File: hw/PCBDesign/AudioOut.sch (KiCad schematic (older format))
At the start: 1 part

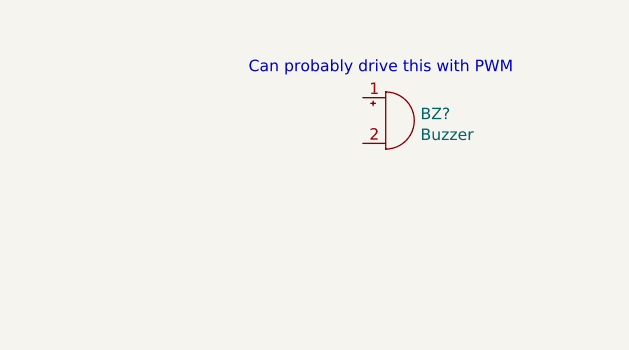
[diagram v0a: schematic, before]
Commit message: Add HMI input circuitry
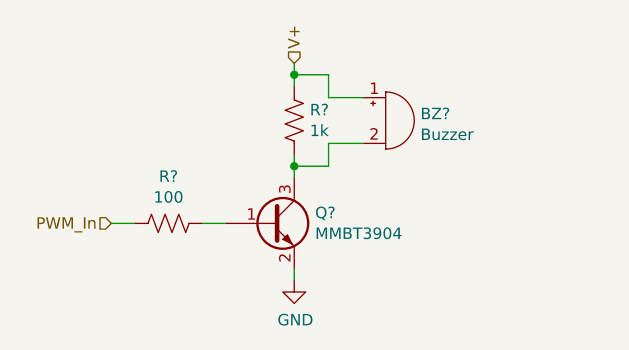
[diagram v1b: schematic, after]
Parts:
- added Q?: MMBT3904, Package_TO_SOT_SMD:SOT-23, symbol Transistor_BJT:MMBT3904
- added R?: 100, symbol Device:R_US
- added R?: 1k, symbol Device:R_US
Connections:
- net V+: now reaches BZ?.1 (-)
- net V+: now also R?.2
- net at BZ?.2 (+): now also Q?.3 (C), R?.1
- new net: Q?.1 (B), R?.1
- new net GND: Q?.2 (E)
- new net PWM_In: R?.2
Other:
- note removed: "Can probably drive this with PWM\n"
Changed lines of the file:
@@
 	1    0    0    -1
 $EndComp
-Text Notes 5350 2700 0    50   ~ 0
-Can probably drive this with PWM\n
+$Comp
+L Transistor_BJT:MMBT3904 Q?
+U 1 1 604D69BF
+P 5450 3350
+F 0 "Q?" H 5641 3396 50  0000 L CNN
+F 1 "MMBT3904" H 5641 3305 50  0000 L CNN
+F 2 "Package_TO_SOT_SMD:SOT-23" H 5650 3275 50  0001 L CIN
+F 3 "https://www.onsemi.com/pub/Collateral/2N3903-D.PDF" H 5450 3350 50  0001 L CNN
+	1    5450 3350
+	1    0    0    -1
+$EndComp
+$Comp
+L Device:R_US R?
+U 1 1 604D79F0
+P 5000 3350
+F 0 "R?" V 4795 3350 50  0000 C CNN
+F 1 "100" V 4886 3350 50  0000 C CNN
+F 2 "" V 5040 3340 50  0001 C CNN
+F 3 "~" H 5000 3350 50  0001 C CNN
+	1    5000 3350
+	0    1    1    0
+$EndComp
+$Comp
+L Device:R_US R?
+U 1 1 604D8132
+P 5550 2900
+F 0 "R?" H 5482 2854 50  0000 R CNN
+F 1 "1k" H 5482 2945 50  0000 R CNN
+F 2 "" V 5590 2890 50  0001 C CNN
+F 3 "~" H 5550 2900 50  0001 C CNN
+	1    5550 2900
+	-1   0    0    1
+$EndComp
+Text HLabel 5550 2650 1    50   Input ~ 0
+V+
+Wire Wire Line
+	5550 2650 5550 2700
+Wire Wire Line
+	5550 3050 5550 3100
+Wire Wire Line
+	5150 3350 5250 3350
+Wire Wire Line
+	5850 2800 5700 2800
+Wire Wire Line
+	5700 2800 5700 2700
+Wire Wire Line
+	5700 2700 5550 2700
+Connection ~ 5550 2700
+Wire Wire Line
+	5550 2700 5550 2750
+Wire Wire Line
+	5850 3000 5700 3000
+Wire Wire Line
+	5700 3000 5700 3100
+Wire Wire Line
+	5700 3100 5550 3100
+Connection ~ 5550 3100
+Wire Wire Line
+	5550 3100 5550 3150
+$Comp
+L power:GND #PWR?
+U 1 1 604DA05E
+P 5550 3600
+F 0 "#PWR?" H 5550 3350 50  0001 C CNN
+F 1 "GND" H 5555 3427 50  0000 C CNN
+F 2 "" H 5550 3600 50  0001 C CNN
+F 3 "" H 5550 3600 50  0001 C CNN
+	1    5550 3600
+	1    0    0    -1
+$EndComp
+Wire Wire Line
+	5550 3550 5550 3600
+Text HLabel 4750 3350 0    50   Input ~ 0
+PWM_In
+Wire Wire Line
+	4750 3350 4850 3350
 $EndSCHEMATC

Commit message: Schematic polishing
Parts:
- BZ1: renamed from BZ?; footprint (none) -> Buzzer_Beeper:Buzzer_12x9.5RM7.6
- Q1: renamed from Q?; LCSC (none) -> C20526
- R43: renamed from R?; footprint (none) -> Resistor_SMD:R_0402_1005Metric; LCSC (none) -> C25076
- R44: renamed from R?; footprint (none) -> Resistor_SMD:R_0402_1005Metric; LCSC (none) -> C11702
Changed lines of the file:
@@
 $EndDescr
 $Comp
-L Device:Buzzer BZ?
+L Device:Buzzer BZ1
 U 1 1 604580F7
 P 5950 2900
-F 0 "BZ?" H 6102 2929 50  0000 L CNN
+F 0 "BZ1" H 6102 2929 50  0000 L CNN
 F 1 "Buzzer" H 6102 2838 50  0000 L CNN
-F 2 "" V 5925 3000 50  0001 C CNN
+F 2 "Buzzer_Beeper:Buzzer_12x9.5RM7.6" V 5925 3000 50  0001 C CNN
 F 3 "~" V 5925 3000 50  0001 C CNN
 	1    5950 2900
@@
 $EndComp
 $Comp
-L Transistor_BJT:MMBT3904 Q?
+L Transistor_BJT:MMBT3904 Q1
 U 1 1 604D69BF
 P 5450 3350
-F 0 "Q?" H 5641 3396 50  0000 L CNN
+F 0 "Q1" H 5641 3396 50  0000 L CNN
 F 1 "MMBT3904" H 5641 3305 50  0000 L CNN
 F 2 "Package_TO_SOT_SMD:SOT-23" H 5650 3275 50  0001 L CIN
 F 3 "https://www.onsemi.com/pub/Collateral/2N3903-D.PDF" H 5450 3350 50  0001 L CNN
+F 4 "C20526" H 5450 3350 50  0001 C CNN "LCSC"
 	1    5450 3350
 	1    0    0    -1
 $EndComp
 $Comp
-L Device:R_US R?
+L Device:R_US R43
 U 1 1 604D79F0
 P 5000 3350
-F 0 "R?" V 4795 3350 50  0000 C CNN
+F 0 "R43" V 4795 3350 50  0000 C CNN
 F 1 "100" V 4886 3350 50  0000 C CNN
-F 2 "" V 5040 3340 50  0001 C CNN
+F 2 "Resistor_SMD:R_0402_1005Metric" V 5040 3340 50  0001 C CNN
 F 3 "~" H 5000 3350 50  0001 C CNN
+F 4 "C25076" H 5000 3350 50  0001 C CNN "LCSC"
 	1    5000 3350
 	0    1    1    0
 $EndComp
 $Comp
-L Device:R_US R?
+L Device:R_US R44
 U 1 1 604D8132
 P 5550 2900
-F 0 "R?" H 5482 2854 50  0000 R CNN
+F 0 "R44" H 5482 2854 50  0000 R CNN
 F 1 "1k" H 5482 2945 50  0000 R CNN
-F 2 "" V 5590 2890 50  0001 C CNN
+F 2 "Resistor_SMD:R_0402_1005Metric" V 5590 2890 50  0001 C CNN
 F 3 "~" H 5550 2900 50  0001 C CNN
+F 4 "C11702" H 5550 2900 50  0001 C CNN "LCSC"
 	1    5550 2900
 	-1   0    0    1
@@
 	5550 3100 5550 3150
 $Comp
-L power:GND #PWR?
+L power:GND #PWR055
 U 1 1 604DA05E
 P 5550 3600
-F 0 "#PWR?" H 5550 3350 50  0001 C CNN
+F 0 "#PWR055" H 5550 3350 50  0001 C CNN
 F 1 "GND" H 5555 3427 50  0000 C CNN
 F 2 "" H 5550 3600 50  0001 C CNN
